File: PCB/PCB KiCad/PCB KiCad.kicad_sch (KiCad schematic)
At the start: 0 parts

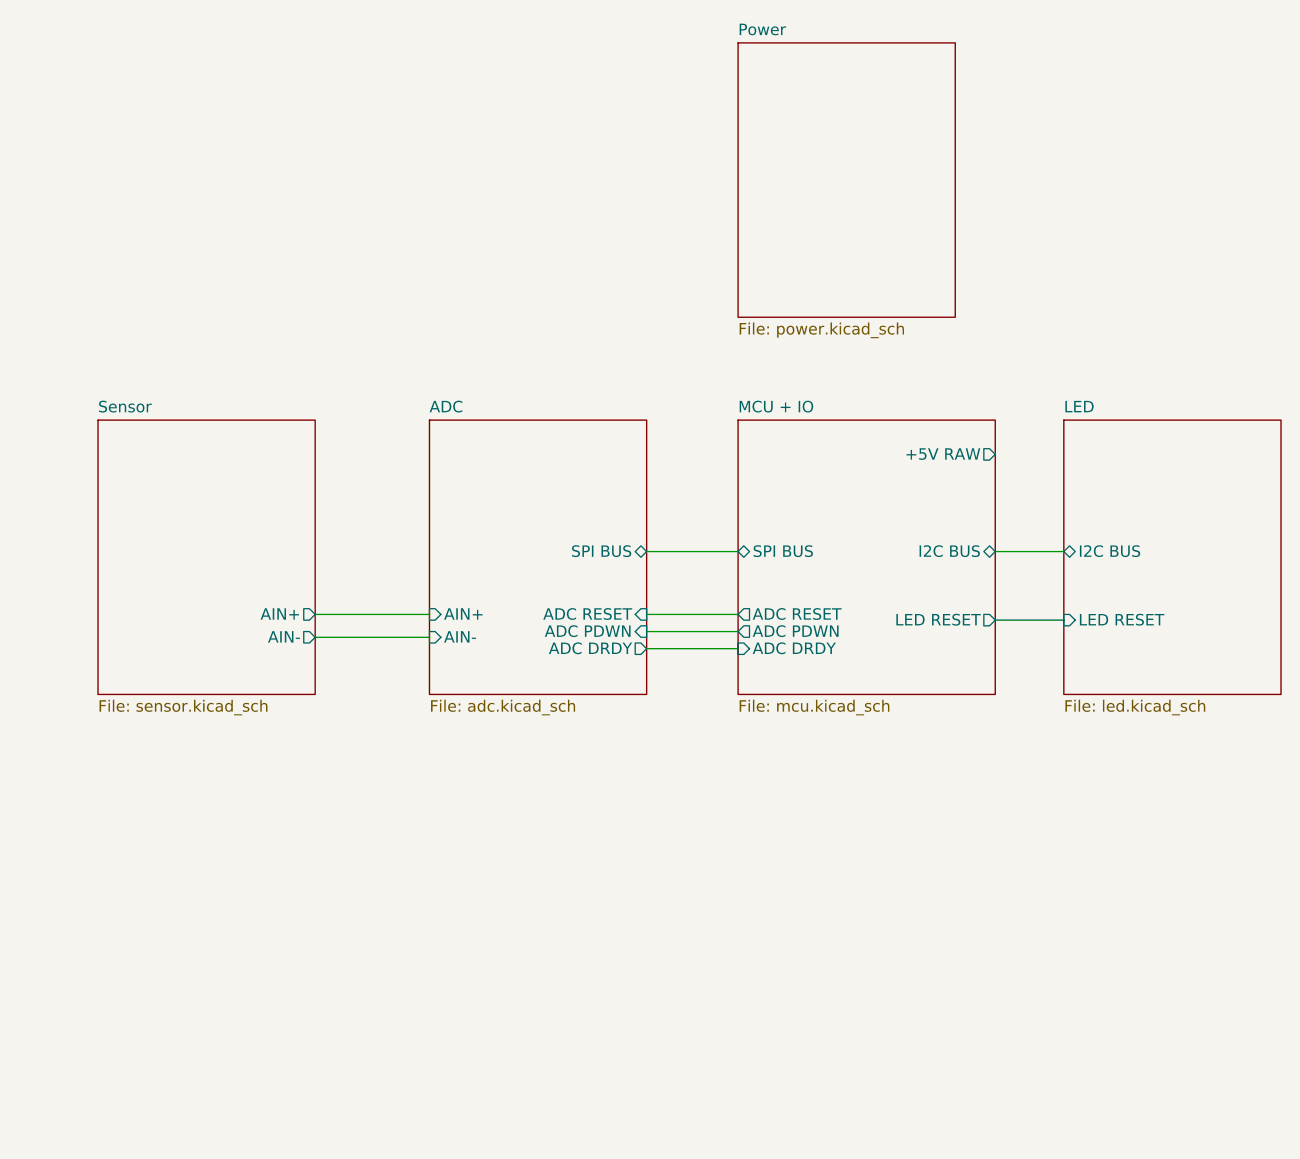
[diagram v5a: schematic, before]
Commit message: Satisfy the overdemanding attention hungry ERC monster
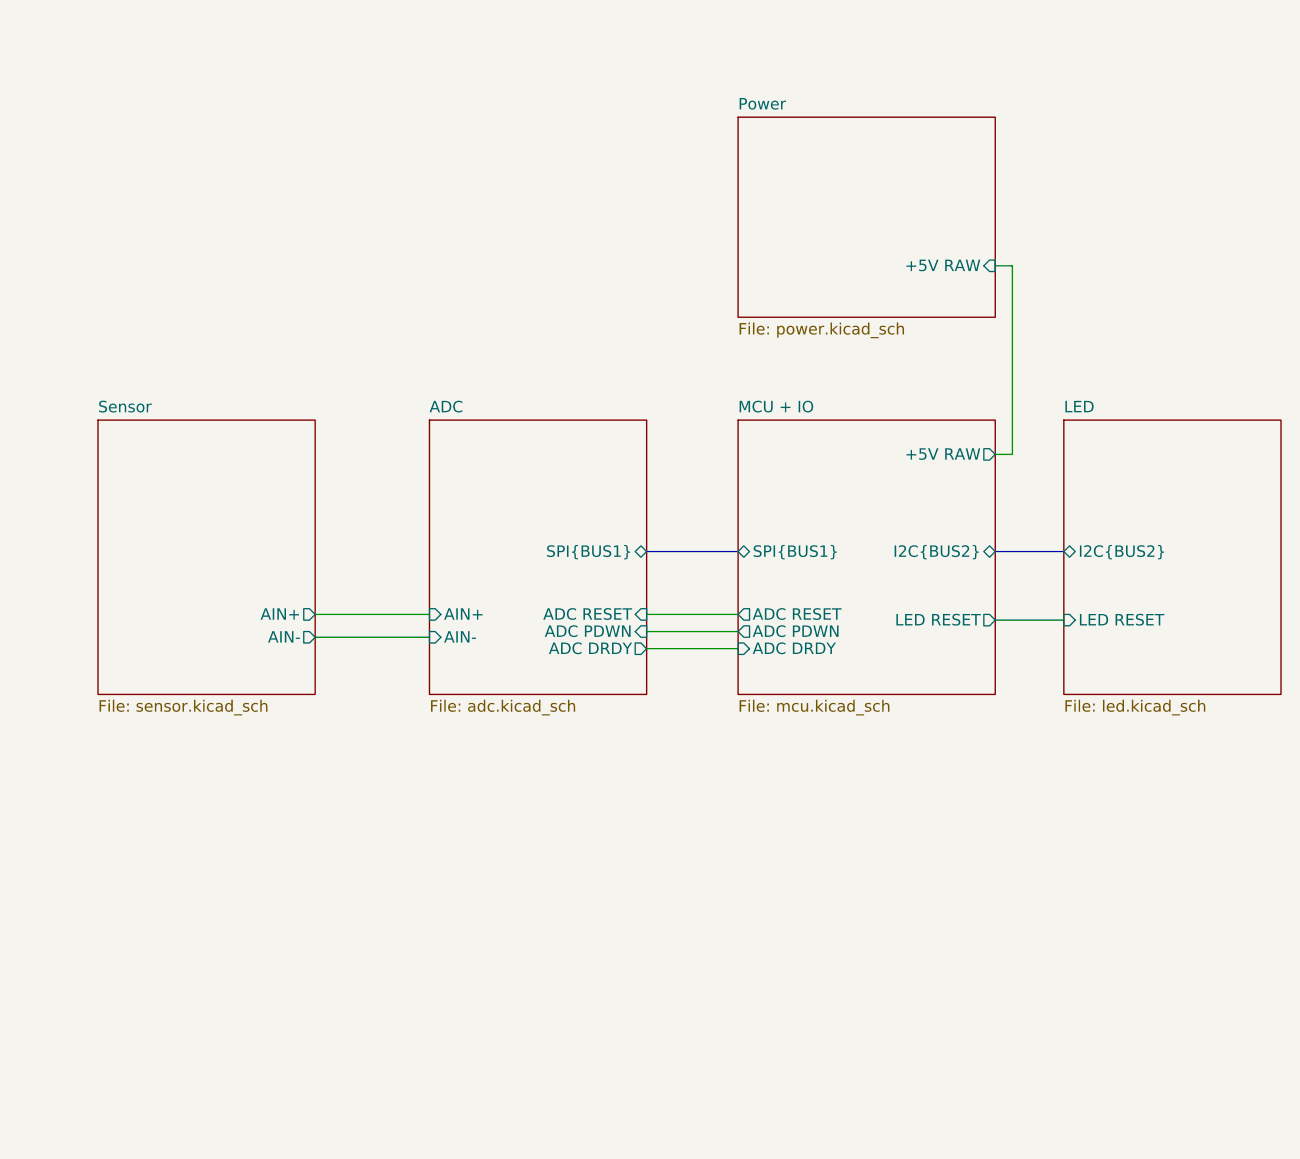
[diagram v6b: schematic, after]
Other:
- sheet ADC ports: added SPI{BUS1}; removed SPI BUS
- sheet LED ports: added I2C{BUS2}; removed I2C BUS
- sheet MCU + IO ports: added I2C{BUS2}, SPI{BUS1}; removed I2C BUS, SPI BUS
- sheet Power ports: added +5V RAW; removed none
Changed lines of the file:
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@@
 (kicad_sch (version 20211123) (generator eeschema)
   (paper "A4")
+  (bus (pts (xy 168.275 92.075) (xy 175.895 92.075))
+    (stroke (width 0) (type default) (color 0 0 0 0))
+  )
   (wire (pts (xy 92.71 99.06) (xy 105.41 99.06))
     (stroke (width 0) (type default) (color 0 0 0 0))
@@
     (stroke (width 0) (type default) (color 0 0 0 0))
   )
+  (wire (pts (xy 168.275 81.28) (xy 170.18 81.28))
+    (stroke (width 0) (type default) (color 0 0 0 0))
+  )
+  (wire (pts (xy 170.18 81.28) (xy 170.18 60.325))
+    (stroke (width 0) (type default) (color 0 0 0 0))
+  )
+  (bus (pts (xy 129.54 92.075) (xy 139.7 92.075))
+    (stroke (width 0) (type default) (color 0 0 0 0))
+  )
+  (wire (pts (xy 168.275 60.325) (xy 170.18 60.325))
+    (stroke (width 0) (type default) (color 0 0 0 0))
+  )
   (wire (pts (xy 168.275 99.695) (xy 175.895 99.695))
     (stroke (width 0) (type default) (color 0 0 0 0))
@@
   )
   (wire (pts (xy 129.54 100.965) (xy 139.7 100.965))
-    (stroke (width 0) (type default) (color 0 0 0 0))
-  )
-  (wire (pts (xy 129.54 92.075) (xy 139.7 92.075))
-    (stroke (width 0) (type default) (color 0 0 0 0))
-  )
-  (wire (pts (xy 168.275 92.075) (xy 175.895 92.075))
     (stroke (width 0) (type default) (color 0 0 0 0))
   )
@@
       (effects (font (size 1.27 1.27)) (justify left))
     )
-    (pin "I2C BUS" bidirectional (at 175.895 92.075 180)
+    (pin "I2C{BUS2}" bidirectional (at 175.895 92.075 180)
       (effects (font (size 1.27 1.27)) (justify left))
     )
   )
-  (sheet (at 139.7 35.56) (size 24.13 30.48) (fields_autoplaced)
+  (sheet (at 139.7 43.815) (size 28.575 22.225) (fields_autoplaced)
     (stroke (width 0.1524) (type solid) (color 0 0 0 0))
     (fill (color 0 0 0 0.0000))
-    (property "Sheet name" "Power" (id 0) (at 139.7 34.8484 0)
+    (property "Sheet name" "Power" (id 0) (at 139.7 43.1034 0)
       (effects (font (size 1.27 1.27)) (justify left bottom))
     )
     (property "Sheet file" "power.kicad_sch" (id 1) (at 139.7 66.6246 0)
       (effects (font (size 1.27 1.27)) (justify left top))
+    )
+    (pin "+5V RAW" input (at 168.275 60.325 0)
+      (effects (font (size 1.27 1.27)) (justify right))
     )
   )
@@
       (effects (font (size 1.27 1.27)) (justify right))
     )
-    (pin "SPI BUS" bidirectional (at 129.54 92.075 0)
+    (pin "SPI{BUS1}" bidirectional (at 129.54 92.075 0)
       (effects (font (size 1.27 1.27)) (justify right))
     )
@@
       (effects (font (size 1.27 1.27)) (justify left top))
     )
-    (pin "SPI BUS" bidirectional (at 139.7 92.075 180)
+    (pin "SPI{BUS1}" bidirectional (at 139.7 92.075 180)
       (effects (font (size 1.27 1.27)) (justify left))
     )
@@
       (effects (font (size 1.27 1.27)) (justify right))
     )
-    (pin "I2C BUS" bidirectional (at 168.275 92.075 0)
+    (pin "I2C{BUS2}" bidirectional (at 168.275 92.075 0)
       (effects (font (size 1.27 1.27)) (justify right))
     )
@@
     )
     (path "/5869e7b3-0d61-455b-97ad-e4e8b4829f27/5502c0bc-fe0c-4e2b-abdd-d0e80e73da9e"
-      (reference "#FLG?") (unit 1) (value "PWR_FLAG") (footprint "")
-    )
-    (path "/5869e7b3-0d61-455b-97ad-e4e8b4829f27/979cd9d8-655c-43a9-9497-f94042a6489d"
-      (reference "#FLG?") (unit 1) (value "PWR_FLAG") (footprint "")
+      (reference "#FLG0104") (unit 1) (value "PWR_FLAG") (footprint "")
     )
     (path "/98df1e87-3735-4cb9-8253-663f6eb2234f/6cc4df4c-9ea0-45fa-baa8-a5dff84d9cc0"
